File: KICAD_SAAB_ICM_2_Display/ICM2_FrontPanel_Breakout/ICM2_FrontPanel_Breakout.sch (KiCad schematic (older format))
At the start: 6 parts, among them J1 Controls_1_29, J2 Controls_Connector, J3 Controls_2_30, J4 Display_Connector, J5 Conn_01x10, J6 Conn_01x10

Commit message: Further refined FFC breakout board, quite happy with this design.
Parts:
- removed J1: Controls_1_29, Connector_PinHeader_2.54mm:PinHeader_1x15_P2.54mm_Vertical, symbol Connector_Generic:Conn_01x15
- removed J3: Controls_2_30, Connector_PinHeader_2.54mm:PinHeader_1x15_P2.54mm_Vertical, symbol Connector_Generic:Conn_01x15
- removed J5, J6: Conn_01x10, Connector_PinHeader_2.54mm:PinHeader_1x10_P2.54mm_Vertical, symbol Connector_Generic:Conn_01x10
- added J1P1, J1P7: P1-5, custom_symbols:PinHeader_1x05_P2.54mm_Vertical_Simple, symbol Connector_Generic:Conn_01x05
- added J1P10, J1P3: P11-15, custom_symbols:PinHeader_1x05_P2.54mm_Vertical_Simple, symbol Connector_Generic:Conn_01x05
- added J1P2, J1P8: P6-10, custom_symbols:PinHeader_1x05_P2.54mm_Vertical_Simple, symbol Connector_Generic:Conn_01x05
- added J1P4: P21-30, custom_symbols:PinHeader_1x05_P2.54mm_Vertical_Simple, symbol Connector_Generic:Conn_01x05
- added J1P5: P21-25, custom_symbols:PinHeader_1x05_P2.54mm_Vertical_Simple, symbol Connector_Generic:Conn_01x05
- added J1P6, J1P9: P16-20, custom_symbols:PinHeader_1x05_P2.54mm_Vertical_Simple, symbol Connector_Generic:Conn_01x05
- J1: renamed from J2; symbol Connector_Generic:Conn_02x15_Odd_Even -> Connector_Generic:Conn_02x15_Counter_Clockwise
- J2: renamed from J4; symbol Connector_Generic_MountingPin:Conn_02x10_Odd_Even_MountingPin -> Connector_Generic:Conn_02x10_Counter_Clockwise
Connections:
- net at J1.1 (Pin_1): now also J1P1.1 (Pin_1)
- net at J1.10 (Pin_10): now also J1P2.5 (Pin_5)
- net at J1.11 (Pin_11): now also J1P3.1 (Pin_1)
- net at J1.12 (Pin_12): now also J1P3.2 (Pin_2)
- net at J1.13 (Pin_13): now also J1P3.3 (Pin_3)
- net at J1.14 (Pin_14): now also J1P3.4 (Pin_4)
- net at J1.15 (Pin_15): now also J1P3.5 (Pin_5)
- net at J1.16 (Pin_16): now also J1P6.1 (Pin_1)
- net at J1.17 (Pin_17): now also J1P6.2 (Pin_2)
- net at J1.18 (Pin_18): now also J1P6.3 (Pin_3)
- net at J1.19 (Pin_19): now also J1P6.4 (Pin_4)
- net at J1.2 (Pin_2): now also J1P1.2 (Pin_2)
- net at J1.20 (Pin_20): now also J1P6.5 (Pin_5)
- net at J1.21 (Pin_21): now also J1P5.1 (Pin_1)
- net at J1.22 (Pin_22): now also J1P5.2 (Pin_2)
- net at J1.23 (Pin_23): now also J1P5.3 (Pin_3)
- net at J1.24 (Pin_24): now also J1P5.4 (Pin_4)
- net at J1.25 (Pin_25): now also J1P5.5 (Pin_5)
- net at J1.26 (Pin_26): now also J1P4.1 (Pin_1)
- net at J1.27 (Pin_27): now also J1P4.2 (Pin_2)
- net at J1.28 (Pin_28): now also J1P4.3 (Pin_3)
- net at J1.29 (Pin_29): now also J1P4.4 (Pin_4)
- net at J1.3 (Pin_3): now also J1P1.3 (Pin_3)
- net at J1.30 (Pin_30): now also J1P4.5 (Pin_5)
- net at J1.4 (Pin_4): now also J1P1.4 (Pin_4)
- net at J1.5 (Pin_5): now also J1P1.5 (Pin_5)
- net at J1.6 (Pin_6): now also J1P2.1 (Pin_1)
- net at J1.7 (Pin_7): now also J1P2.2 (Pin_2)
- net at J1.8 (Pin_8): now also J1P2.3 (Pin_3)
- net at J1.9 (Pin_9): now also J1P2.4 (Pin_4)
- net at J2.1 (Pin_1): now also J1P7.1 (Pin_1)
- net at J2.19 (Pin_19): now also J1P9.4 (Pin_4)
- net at J2.3 (Pin_3): now also J1P7.3 (Pin_3)
- net at J2.5 (Pin_5): now also J1P7.5 (Pin_5)
- net at J2.7 (Pin_7): now also J1P8.2 (Pin_2)
- net at J2.9 (Pin_9): now also J1P8.4 (Pin_4)
- net at J2.11 (Pin_11): now also J1P10.1 (Pin_1)
- net at J2.13 (Pin_13): now also J1P10.3 (Pin_3)
- net at J2.15 (Pin_15): now also J1P10.5 (Pin_5)
- net at J2.17 (Pin_17): now also J1P9.2 (Pin_2)
- net at J2.2 (Pin_2): now also J1P7.2 (Pin_2)
- net at J2.20 (Pin_20): now also J1P9.5 (Pin_5)
- net at J2.4 (Pin_4): now also J1P7.4 (Pin_4)
- net at J2.6 (Pin_6): now also J1P8.1 (Pin_1)
- net at J2.8 (Pin_8): now also J1P8.3 (Pin_3)
- net at J2.10 (Pin_10): now also J1P8.5 (Pin_5)
- net at J2.12 (Pin_12): now also J1P10.2 (Pin_2)
- net at J2.14 (Pin_14): now also J1P10.4 (Pin_4)
- net at J2.16 (Pin_16): now also J1P9.1 (Pin_1)
- net at J2.18 (Pin_18): now also J1P9.3 (Pin_3)
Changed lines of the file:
@@
 $EndDescr
 $Comp
-L Connector_Generic_MountingPin:Conn_02x10_Odd_Even_MountingPin J4
+L Connector_Generic:Conn_02x10_Counter_Clockwise J2
 U 1 1 5EB8DD98
-P 5650 3300
-F 0 "J4" H 5700 3917 50  0000 C CNN
-F 1 "Display_Connector" H 5700 3826 50  0000 C CNN
-F 2 "Connector_FFC-FPC:Hirose_FH12-20S-0.5SH_1x20-1MP_P0.50mm_Horizontal" H 5650 3300 50  0001 C CNN
-F 3 "~" H 5650 3300 50  0001 C CNN
-	1    5650 3300
+P 6300 3300
+F 0 "J2" H 6350 3950 50  0000 C CNN
+F 1 "Display_Connector" H 6350 3850 50  0000 C CNN
+F 2 "Connector_FFC-FPC:Hirose_FH12-20S-0.5SH_1x20-1MP_P0.50mm_Horizontal" H 6300 3300 50  0001 C CNN
+F 3 "~" H 6300 3300 50  0001 C CNN
+	1    6300 3300
 	1    0    0    -1
 $EndComp
 $Comp
-L Connector_Generic:Conn_02x15_Odd_Even J2
+L Connector_Generic:Conn_02x15_Counter_Clockwise J1
 U 1 1 5EB5BB1D
 P 4400 3350
-F 0 "J2" H 4450 4267 50  0000 C CNN
-F 1 "Controls_Connector" H 4450 4176 50  0000 C CNN
+F 0 "J1" H 4450 4350 50  0000 C CNN
+F 1 "Controls_Connector" H 4450 4250 50  0000 C CNN
 F 2 "Connector_FFC-FPC:Hirose_FH12-30S-0.5SH_1x30-1MP_P0.50mm_Horizontal" H 4400 3350 50  0001 C CNN
 F 3 "~" H 4400 3350 50  0001 C CNN
@@
 $EndComp
 $Comp
-L Connector_Generic:Conn_01x15 J1
-U 1 1 5EB6A081
+L Connector_Generic:Conn_01x05 J1P1
+U 1 1 5EC714E0
+P 4000 2850
+F 0 "J1P1" H 4300 3050 50  0000 R CNN
+F 1 "P1-5" H 4300 2950 50  0000 R CNN
+F 2 "custom_symbols:PinHeader_1x05_P2.54mm_Vertical_Simple" H 4000 2850 50  0001 C CNN
+F 3 "~" H 4000 2850 50  0001 C CNN
+	1    4000 2850
+	-1   0    0    -1
+$EndComp
+$Comp
+L Connector_Generic:Conn_01x05 J1P2
+U 1 1 5EC8CD34
 P 4000 3350
-F 0 "J1" H 3950 2500 50  0000 L CNN
-F 1 "Controls_1_29" H 3950 2400 50  0000 L CNN
-F 2 "Connector_PinHeader_2.54mm:PinHeader_1x15_P2.54mm_Vertical" H 4000 3350 50  0001 C CNN
+F 0 "J1P2" H 4300 3550 50  0000 R CNN
+F 1 "P6-10" H 4350 3450 50  0000 R CNN
+F 2 "custom_symbols:PinHeader_1x05_P2.54mm_Vertical_Simple" H 4000 3350 50  0001 C CNN
 F 3 "~" H 4000 3350 50  0001 C CNN
 	1    4000 3350
@@
 $EndComp
 $Comp
-L Connector_Generic:Conn_01x15 J3
-U 1 1 5EB6A85F
-P 4900 3350
-F 0 "J3" H 4818 2425 50  0000 C CNN
-F 1 "Controls_2_30" H 4700 2500 50  0000 C CNN
-F 2 "Connector_PinHeader_2.54mm:PinHeader_1x15_P2.54mm_Vertical" H 4900 3350 50  0001 C CNN
-F 3 "~" H 4900 3350 50  0001 C CNN
-	1    4900 3350
-	1    0    0    -1
-$EndComp
-$Comp
-L Connector_Generic:Conn_01x10 J5
-U 1 1 5EB771C1
-P 5250 3300
-F 0 "J5" H 5168 3917 50  0000 C CNN
-F 1 "Conn_01x10" H 5168 3826 50  0000 C CNN
-F 2 "Connector_PinHeader_2.54mm:PinHeader_1x10_P2.54mm_Vertical" H 5250 3300 50  0001 C CNN
-F 3 "~" H 5250 3300 50  0001 C CNN
-	1    5250 3300
+L Connector_Generic:Conn_01x05 J1P3
+U 1 1 5EC8D57C
+P 4000 3850
+F 0 "J1P3" H 4300 4050 50  0000 R CNN
+F 1 "P11-15" H 4400 3950 50  0000 R CNN
+F 2 "custom_symbols:PinHeader_1x05_P2.54mm_Vertical_Simple" H 4000 3850 50  0001 C CNN
+F 3 "~" H 4000 3850 50  0001 C CNN
+	1    4000 3850
 	-1   0    0    -1
 $EndComp
 $Comp
-L Connector_Generic:Conn_01x10 J6
-U 1 1 5EB7A8B0
-P 6150 3300
-F 0 "J6" H 6230 3292 50  0000 L CNN
-F 1 "Conn_01x10" H 6230 3201 50  0000 L CNN
-F 2 "Connector_PinHeader_2.54mm:PinHeader_1x10_P2.54mm_Vertical" H 6150 3300 50  0001 C CNN
-F 3 "~" H 6150 3300 50  0001 C CNN
-	1    6150 3300
-	1    0    0    -1
+L Connector_Generic:Conn_01x05 J1P6
+U 1 1 5EC94131
+P 4900 3850
+F 0 "J1P6" H 5200 4050 50  0000 R CNN
+F 1 "P16-20" H 5300 3950 50  0000 R CNN
+F 2 "custom_symbols:PinHeader_1x05_P2.54mm_Vertical_Simple" H 4900 3850 50  0001 C CNN
+F 3 "~" H 4900 3850 50  0001 C CNN
+	1    4900 3850
+	1    0    0    1
+$EndComp
+$Comp
+L Connector_Generic:Conn_01x05 J1P5
+U 1 1 5EC94137
+P 4900 3350
+F 0 "J1P5" H 5200 3550 50  0000 R CNN
+F 1 "P21-25" H 5300 3450 50  0000 R CNN
+F 2 "custom_symbols:PinHeader_1x05_P2.54mm_Vertical_Simple" H 4900 3350 50  0001 C CNN
+F 3 "~" H 4900 3350 50  0001 C CNN
+	1    4900 3350
+	1    0    0    1
+$EndComp
+$Comp
+L Connector_Generic:Conn_01x05 J1P4
+U 1 1 5EC9413D
+P 4900 2850
+F 0 "J1P4" H 5200 3050 50  0000 R CNN
+F 1 "P21-30" H 5300 2950 50  0000 R CNN
+F 2 "custom_symbols:PinHeader_1x05_P2.54mm_Vertical_Simple" H 4900 2850 50  0001 C CNN
+F 3 "~" H 4900 2850 50  0001 C CNN
+	1    4900 2850
+	1    0    0    1
+$EndComp
+$Comp
+L Connector_Generic:Conn_01x05 J1P7
+U 1 1 5EC9B345
+P 5900 3100
+F 0 "J1P7" H 6200 3300 50  0000 R CNN
+F 1 "P1-5" H 6200 3200 50  0000 R CNN
+F 2 "custom_symbols:PinHeader_1x05_P2.54mm_Vertical_Simple" H 5900 3100 50  0001 C CNN
+F 3 "~" H 5900 3100 50  0001 C CNN
+	1    5900 3100
+	-1   0    0    -1
+$EndComp
+$Comp
+L Connector_Generic:Conn_01x05 J1P8
+U 1 1 5EC9B34B
+P 5900 3600
+F 0 "J1P8" H 6200 3800 50  0000 R CNN
+F 1 "P6-10" H 6250 3700 50  0000 R CNN
+F 2 "custom_symbols:PinHeader_1x05_P2.54mm_Vertical_Simple" H 5900 3600 50  0001 C CNN
+F 3 "~" H 5900 3600 50  0001 C CNN
+	1    5900 3600
+	-1   0    0    -1
+$EndComp
+$Comp
+L Connector_Generic:Conn_01x05 J1P10
+U 1 1 5ECA16B9
+P 6800 3600
+F 0 "J1P10" H 7100 3800 50  0000 R CNN
+F 1 "P11-15" H 7200 3700 50  0000 R CNN
+F 2 "custom_symbols:PinHeader_1x05_P2.54mm_Vertical_Simple" H 6800 3600 50  0001 C CNN
+F 3 "~" H 6800 3600 50  0001 C CNN
+	1    6800 3600
+	1    0    0    1
+$EndComp
+$Comp
+L Connector_Generic:Conn_01x05 J1P9
+U 1 1 5ECA16BF
+P 6800 3100
+F 0 "J1P9" H 7100 3300 50  0000 R CNN
+F 1 "P16-20" H 7200 3200 50  0000 R CNN
+F 2 "custom_symbols:PinHeader_1x05_P2.54mm_Vertical_Simple" H 6800 3100 50  0001 C CNN
+F 3 "~" H 6800 3100 50  0001 C CNN
+	1    6800 3100
+	1    0    0    1
 $EndComp
 $EndSCHEMATC

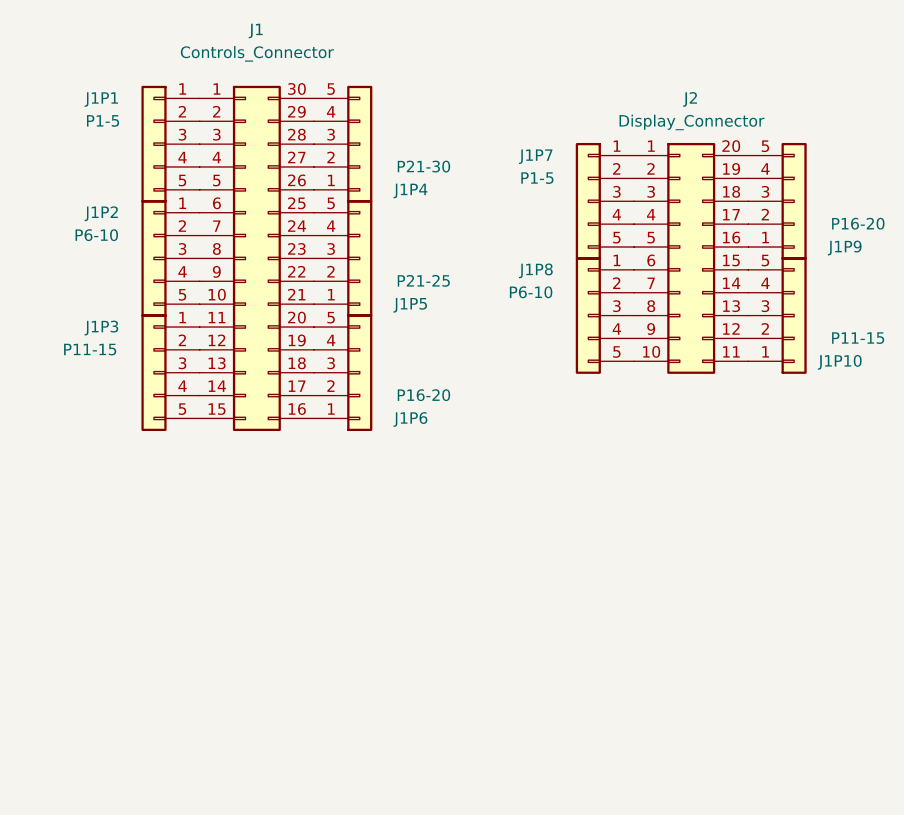
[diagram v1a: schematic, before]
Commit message: Experimenting with alternate style breakout for FFC cables
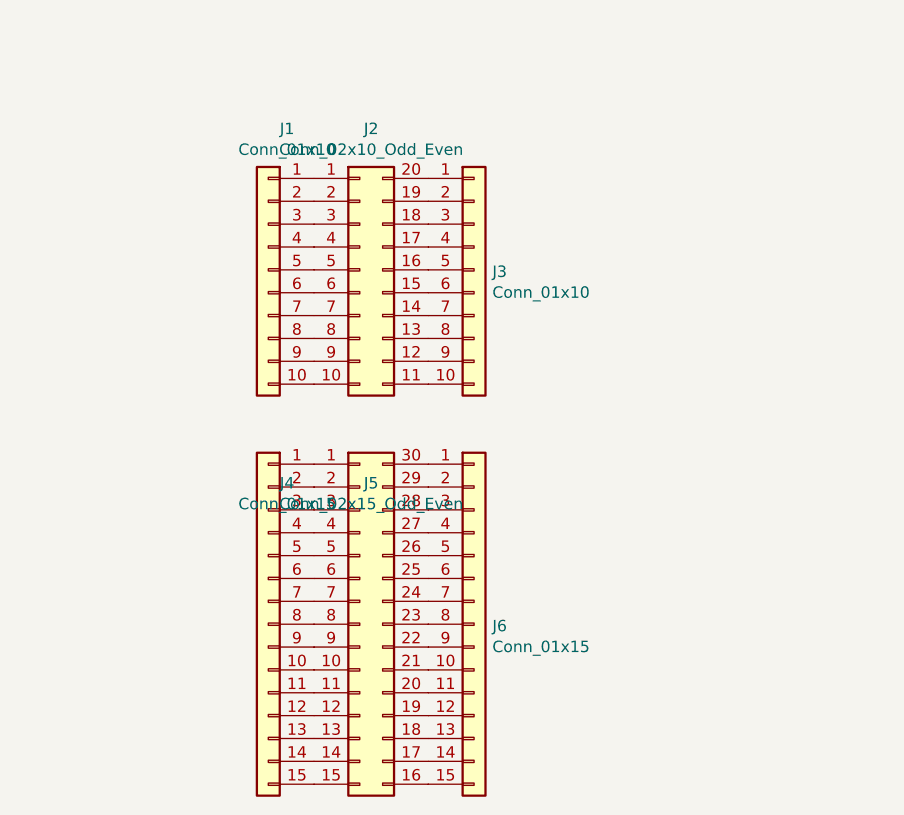
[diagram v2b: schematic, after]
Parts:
- removed J1: Controls_Connector, Connector_FFC-FPC:Hirose_FH12-30S-0.5SH_1x30-1MP_P0.50mm_Horizontal, symbol Connector_Generic:Conn_02x15_Counter_Clockwise
- removed J1P1, J1P7: P1-5, custom_symbols:PinHeader_1x05_P2.54mm_Vertical_Simple, symbol Connector_Generic:Conn_01x05
- removed J1P10, J1P3: P11-15, custom_symbols:PinHeader_1x05_P2.54mm_Vertical_Simple, symbol Connector_Generic:Conn_01x05
- removed J1P2, J1P8: P6-10, custom_symbols:PinHeader_1x05_P2.54mm_Vertical_Simple, symbol Connector_Generic:Conn_01x05
- removed J1P4: P21-30, custom_symbols:PinHeader_1x05_P2.54mm_Vertical_Simple, symbol Connector_Generic:Conn_01x05
- removed J1P5: P21-25, custom_symbols:PinHeader_1x05_P2.54mm_Vertical_Simple, symbol Connector_Generic:Conn_01x05
- removed J1P6, J1P9: P16-20, custom_symbols:PinHeader_1x05_P2.54mm_Vertical_Simple, symbol Connector_Generic:Conn_01x05
- added J1, J3: Conn_01x10, Connector_PinSocket_2.54mm:PinSocket_1x10_P2.54mm_Vertical_SMD_Pin1Left, symbol Connector_Generic:Conn_01x10
- added J4, J6: Conn_01x15, Connector_PinSocket_2.54mm:PinSocket_1x15_P2.54mm_Vertical_SMD_Pin1Left, symbol Connector_Generic:Conn_01x15
- added J5: Conn_02x15_Odd_Even, Connector_FFC-FPC:Hirose_FH12-30S-0.5SH_1x30-1MP_P0.50mm_Horizontal, symbol Connector_Generic:Conn_02x15_Counter_Clockwise
- J2: value Display_Connector -> Conn_02x10_Odd_Even
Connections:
- net at J2.1 (Pin_1): now also J1.1 (Pin_1)
- net at J2.10 (Pin_10): now also J1.10 (Pin_10)
- net at J2.11 (Pin_11): now also J3.10 (Pin_10)
- net at J2.12 (Pin_12): now also J3.9 (Pin_9)
- net at J2.13 (Pin_13): now also J3.8 (Pin_8)
- net at J2.14 (Pin_14): now also J3.7 (Pin_7)
- net at J2.15 (Pin_15): now also J3.6 (Pin_6)
- net at J2.16 (Pin_16): now also J3.5 (Pin_5)
- net at J2.17 (Pin_17): now also J3.4 (Pin_4)
- net at J2.18 (Pin_18): now also J3.3 (Pin_3)
- net at J2.19 (Pin_19): now also J3.2 (Pin_2)
- net at J2.2 (Pin_2): now also J1.2 (Pin_2)
- net at J2.20 (Pin_20): now also J3.1 (Pin_1)
- net at J2.3 (Pin_3): now also J1.3 (Pin_3)
- net at J2.4 (Pin_4): now also J1.4 (Pin_4)
- net at J2.5 (Pin_5): now also J1.5 (Pin_5)
- net at J2.6 (Pin_6): now also J1.6 (Pin_6)
- net at J2.7 (Pin_7): now also J1.7 (Pin_7)
- net at J2.8 (Pin_8): now also J1.8 (Pin_8)
- net at J2.9 (Pin_9): now also J1.9 (Pin_9)
- new net: J4.1 (Pin_1), J5.1 (Pin_1)
- new net: J4.10 (Pin_10), J5.10 (Pin_10)
- new net: J4.11 (Pin_11), J5.11 (Pin_11)
- new net: J4.12 (Pin_12), J5.12 (Pin_12)
- new net: J4.13 (Pin_13), J5.13 (Pin_13)
- new net: J4.14 (Pin_14), J5.14 (Pin_14)
- new net: J4.15 (Pin_15), J5.15 (Pin_15)
- new net: J5.16 (Pin_16), J6.15 (Pin_15)
- new net: J5.17 (Pin_17), J6.14 (Pin_14)
- new net: J5.18 (Pin_18), J6.13 (Pin_13)
- new net: J5.19 (Pin_19), J6.12 (Pin_12)
- new net: J4.2 (Pin_2), J5.2 (Pin_2)
- new net: J5.20 (Pin_20), J6.11 (Pin_11)
- new net: J5.21 (Pin_21), J6.10 (Pin_10)
- new net: J5.22 (Pin_22), J6.9 (Pin_9)
- new net: J5.23 (Pin_23), J6.8 (Pin_8)
- new net: J5.24 (Pin_24), J6.7 (Pin_7)
- new net: J5.25 (Pin_25), J6.6 (Pin_6)
- new net: J5.26 (Pin_26), J6.5 (Pin_5)
- new net: J5.27 (Pin_27), J6.4 (Pin_4)
- new net: J5.28 (Pin_28), J6.3 (Pin_3)
- new net: J5.29 (Pin_29), J6.2 (Pin_2)
- new net: J4.3 (Pin_3), J5.3 (Pin_3)
- new net: J5.30 (Pin_30), J6.1 (Pin_1)
- new net: J4.4 (Pin_4), J5.4 (Pin_4)
- new net: J4.5 (Pin_5), J5.5 (Pin_5)
- new net: J4.6 (Pin_6), J5.6 (Pin_6)
- new net: J4.7 (Pin_7), J5.7 (Pin_7)
- new net: J4.8 (Pin_8), J5.8 (Pin_8)
- new net: J4.9 (Pin_9), J5.9 (Pin_9)
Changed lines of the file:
@@
 $Comp
 L Connector_Generic:Conn_02x10_Counter_Clockwise J2
-U 1 1 5EB8DD98
-P 6300 3300
-F 0 "J2" H 6350 3950 50  0000 C CNN
-F 1 "Display_Connector" H 6350 3850 50  0000 C CNN
-F 2 "Connector_FFC-FPC:Hirose_FH12-20S-0.5SH_1x20-1MP_P0.50mm_Horizontal" H 6300 3300 50  0001 C CNN
-F 3 "~" H 6300 3300 50  0001 C CNN
-	1    6300 3300
+U 1 1 5F3D8984
+P 4900 3400
+F 0 "J2" H 4950 4017 50  0000 C CNN
+F 1 "Conn_02x10_Odd_Even" H 4950 3926 50  0000 C CNN
+F 2 "Connector_FFC-FPC:Hirose_FH12-20S-0.5SH_1x20-1MP_P0.50mm_Horizontal" H 4900 3400 50  0001 C CNN
+F 3 "~" H 4900 3400 50  0001 C CNN
+	1    4900 3400
 	1    0    0    -1
 $EndComp
 $Comp
-L Connector_Generic:Conn_02x15_Counter_Clockwise J1
-U 1 1 5EB5BB1D
-P 4400 3350
-F 0 "J1" H 4450 4350 50  0000 C CNN
-F 1 "Controls_Connector" H 4450 4250 50  0000 C CNN
-F 2 "Connector_FFC-FPC:Hirose_FH12-30S-0.5SH_1x30-1MP_P0.50mm_Horizontal" H 4400 3350 50  0001 C CNN
-F 3 "~" H 4400 3350 50  0001 C CNN
-	1    4400 3350
+L Connector_Generic:Conn_01x10 J3
+U 1 1 5F3DF012
+P 5400 3400
+F 0 "J3" H 5480 3392 50  0000 L CNN
+F 1 "Conn_01x10" H 5480 3301 50  0000 L CNN
+F 2 "Connector_PinSocket_2.54mm:PinSocket_1x10_P2.54mm_Vertical_SMD_Pin1Left" H 5400 3400 50  0001 C CNN
+F 3 "~" H 5400 3400 50  0001 C CNN
+	1    5400 3400
 	1    0    0    -1
 $EndComp
 $Comp
-L Connector_Generic:Conn_01x05 J1P1
-U 1 1 5EC714E0
-P 4000 2850
-F 0 "J1P1" H 4300 3050 50  0000 R CNN
-F 1 "P1-5" H 4300 2950 50  0000 R CNN
-F 2 "custom_symbols:PinHeader_1x05_P2.54mm_Vertical_Simple" H 4000 2850 50  0001 C CNN
-F 3 "~" H 4000 2850 50  0001 C CNN
-	1    4000 2850
+L Connector_Generic:Conn_01x10 J1
+U 1 1 5F3DFA5C
+P 4500 3400
+F 0 "J1" H 4418 4017 50  0000 C CNN
+F 1 "Conn_01x10" H 4418 3926 50  0000 C CNN
+F 2 "Connector_PinSocket_2.54mm:PinSocket_1x10_P2.54mm_Vertical_SMD_Pin1Left" H 4500 3400 50  0001 C CNN
+F 3 "~" H 4500 3400 50  0001 C CNN
+	1    4500 3400
 	-1   0    0    -1
 $EndComp
 $Comp
-L Connector_Generic:Conn_01x05 J1P2
-U 1 1 5EC8CD34
-P 4000 3350
-F 0 "J1P2" H 4300 3550 50  0000 R CNN
-F 1 "P6-10" H 4350 3450 50  0000 R CNN
-F 2 "custom_symbols:PinHeader_1x05_P2.54mm_Vertical_Simple" H 4000 3350 50  0001 C CNN
-F 3 "~" H 4000 3350 50  0001 C CNN
-	1    4000 3350
+L Connector_Generic:Conn_02x15_Counter_Clockwise J5
+U 1 1 5F3EB48E
+P 4900 4950
+F 0 "J5" H 4950 5567 50  0000 C CNN
+F 1 "Conn_02x15_Odd_Even" H 4950 5476 50  0000 C CNN
+F 2 "Connector_FFC-FPC:Hirose_FH12-30S-0.5SH_1x30-1MP_P0.50mm_Horizontal" H 4900 4950 50  0001 C CNN
+F 3 "~" H 4900 4950 50  0001 C CNN
+	1    4900 4950
+	1    0    0    -1
+$EndComp
+$Comp
+L Connector_Generic:Conn_01x15 J6
+U 1 1 5F3EB494
+P 5400 4950
+F 0 "J6" H 5480 4942 50  0000 L CNN
+F 1 "Conn_01x15" H 5480 4851 50  0000 L CNN
+F 2 "Connector_PinSocket_2.54mm:PinSocket_1x15_P2.54mm_Vertical_SMD_Pin1Left" H 5400 4950 50  0001 C CNN
+F 3 "~" H 5400 4950 50  0001 C CNN
+	1    5400 4950
+	1    0    0    -1
+$EndComp
+$Comp
+L Connector_Generic:Conn_01x15 J4
+U 1 1 5F3EB49A
+P 4500 4950
+F 0 "J4" H 4418 5567 50  0000 C CNN
+F 1 "Conn_01x15" H 4418 5476 50  0000 C CNN
+F 2 "Connector_PinSocket_2.54mm:PinSocket_1x15_P2.54mm_Vertical_SMD_Pin1Left" H 4500 4950 50  0001 C CNN
+F 3 "~" H 4500 4950 50  0001 C CNN
+	1    4500 4950
 	-1   0    0    -1
 $EndComp
-$Comp
-L Connector_Generic:Conn_01x05 J1P3
-U 1 1 5EC8D57C
-P 4000 3850
-F 0 "J1P3" H 4300 4050 50  0000 R CNN
-F 1 "P11-15" H 4400 3950 50  0000 R CNN
-F 2 "custom_symbols:PinHeader_1x05_P2.54mm_Vertical_Simple" H 4000 3850 50  0001 C CNN
-F 3 "~" H 4000 3850 50  0001 C CNN
-	1    4000 3850
-	-1   0    0    -1
-$EndComp
-$Comp
-L Connector_Generic:Conn_01x05 J1P6
-U 1 1 5EC94131
-P 4900 3850
-F 0 "J1P6" H 5200 4050 50  0000 R CNN
-F 1 "P16-20" H 5300 3950 50  0000 R CNN
-F 2 "custom_symbols:PinHeader_1x05_P2.54mm_Vertical_Simple" H 4900 3850 50  0001 C CNN
-F 3 "~" H 4900 3850 50  0001 C CNN
-	1    4900 3850
-	1    0    0    1
-$EndComp
-$Comp
-L Connector_Generic:Conn_01x05 J1P5
-U 1 1 5EC94137
-P 4900 3350
-F 0 "J1P5" H 5200 3550 50  0000 R CNN
-F 1 "P21-25" H 5300 3450 50  0000 R CNN
-F 2 "custom_symbols:PinHeader_1x05_P2.54mm_Vertical_Simple" H 4900 3350 50  0001 C CNN
-F 3 "~" H 4900 3350 50  0001 C CNN
-	1    4900 3350
-	1    0    0    1
-$EndComp
-$Comp
-L Connector_Generic:Conn_01x05 J1P4
-U 1 1 5EC9413D
-P 4900 2850
-F 0 "J1P4" H 5200 3050 50  0000 R CNN
-F 1 "P21-30" H 5300 2950 50  0000 R CNN
-F 2 "custom_symbols:PinHeader_1x05_P2.54mm_Vertical_Simple" H 4900 2850 50  0001 C CNN
-F 3 "~" H 4900 2850 50  0001 C CNN
-	1    4900 2850
-	1    0    0    1
-$EndComp
-$Comp
-L Connector_Generic:Conn_01x05 J1P7
-U 1 1 5EC9B345
-P 5900 3100
-F 0 "J1P7" H 6200 3300 50  0000 R CNN
-F 1 "P1-5" H 6200 3200 50  0000 R CNN
-F 2 "custom_symbols:PinHeader_1x05_P2.54mm_Vertical_Simple" H 5900 3100 50  0001 C CNN
-F 3 "~" H 5900 3100 50  0001 C CNN
-	1    5900 3100
-	-1   0    0    -1
-$EndComp
-$Comp
-L Connector_Generic:Conn_01x05 J1P8
-U 1 1 5EC9B34B
-P 5900 3600
-F 0 "J1P8" H 6200 3800 50  0000 R CNN
-F 1 "P6-10" H 6250 3700 50  0000 R CNN
-F 2 "custom_symbols:PinHeader_1x05_P2.54mm_Vertical_Simple" H 5900 3600 50  0001 C CNN
-F 3 "~" H 5900 3600 50  0001 C CNN
-	1    5900 3600
-	-1   0    0    -1
-$EndComp
-$Comp
-L Connector_Generic:Conn_01x05 J1P10
-U 1 1 5ECA16B9
-P 6800 3600
-F 0 "J1P10" H 7100 3800 50  0000 R CNN
-F 1 "P11-15" H 7200 3700 50  0000 R CNN
-F 2 "custom_symbols:PinHeader_1x05_P2.54mm_Vertical_Simple" H 6800 3600 50  0001 C CNN
-F 3 "~" H 6800 3600 50  0001 C CNN
-	1    6800 3600
-	1    0    0    1
-$EndComp
-$Comp
-L Connector_Generic:Conn_01x05 J1P9
-U 1 1 5ECA16BF
-P 6800 3100
-F 0 "J1P9" H 7100 3300 50  0000 R CNN
-F 1 "P16-20" H 7200 3200 50  0000 R CNN
-F 2 "custom_symbols:PinHeader_1x05_P2.54mm_Vertical_Simple" H 6800 3100 50  0001 C CNN
-F 3 "~" H 6800 3100 50  0001 C CNN
-	1    6800 3100
-	1    0    0    1
-$EndComp
 $EndSCHEMATC
